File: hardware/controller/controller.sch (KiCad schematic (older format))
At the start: 7 parts

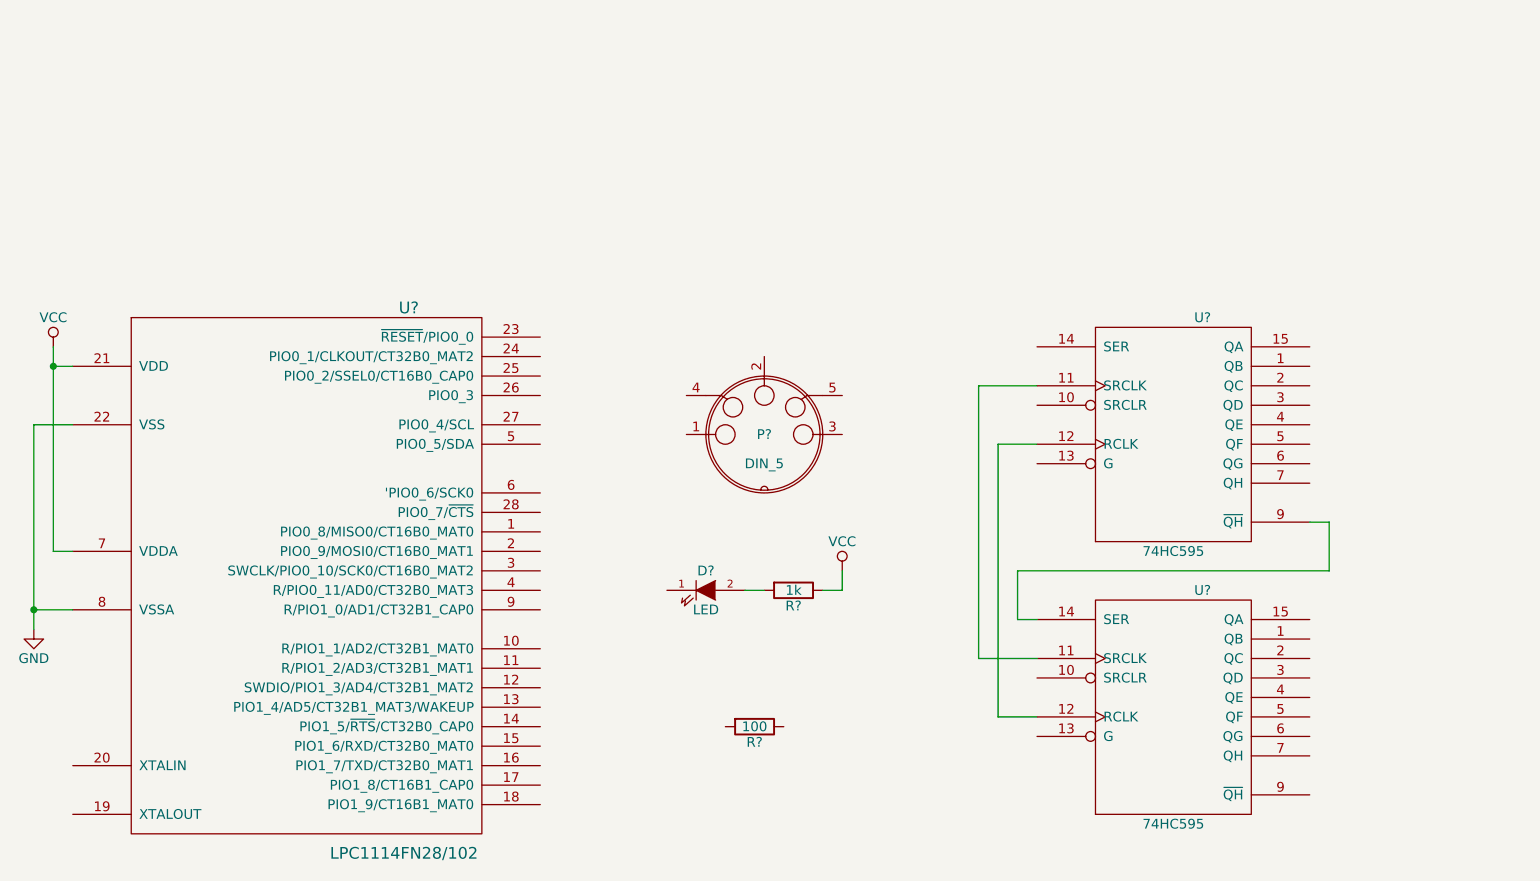
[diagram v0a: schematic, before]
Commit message: Add MIDI input and solenoid drive circuitry
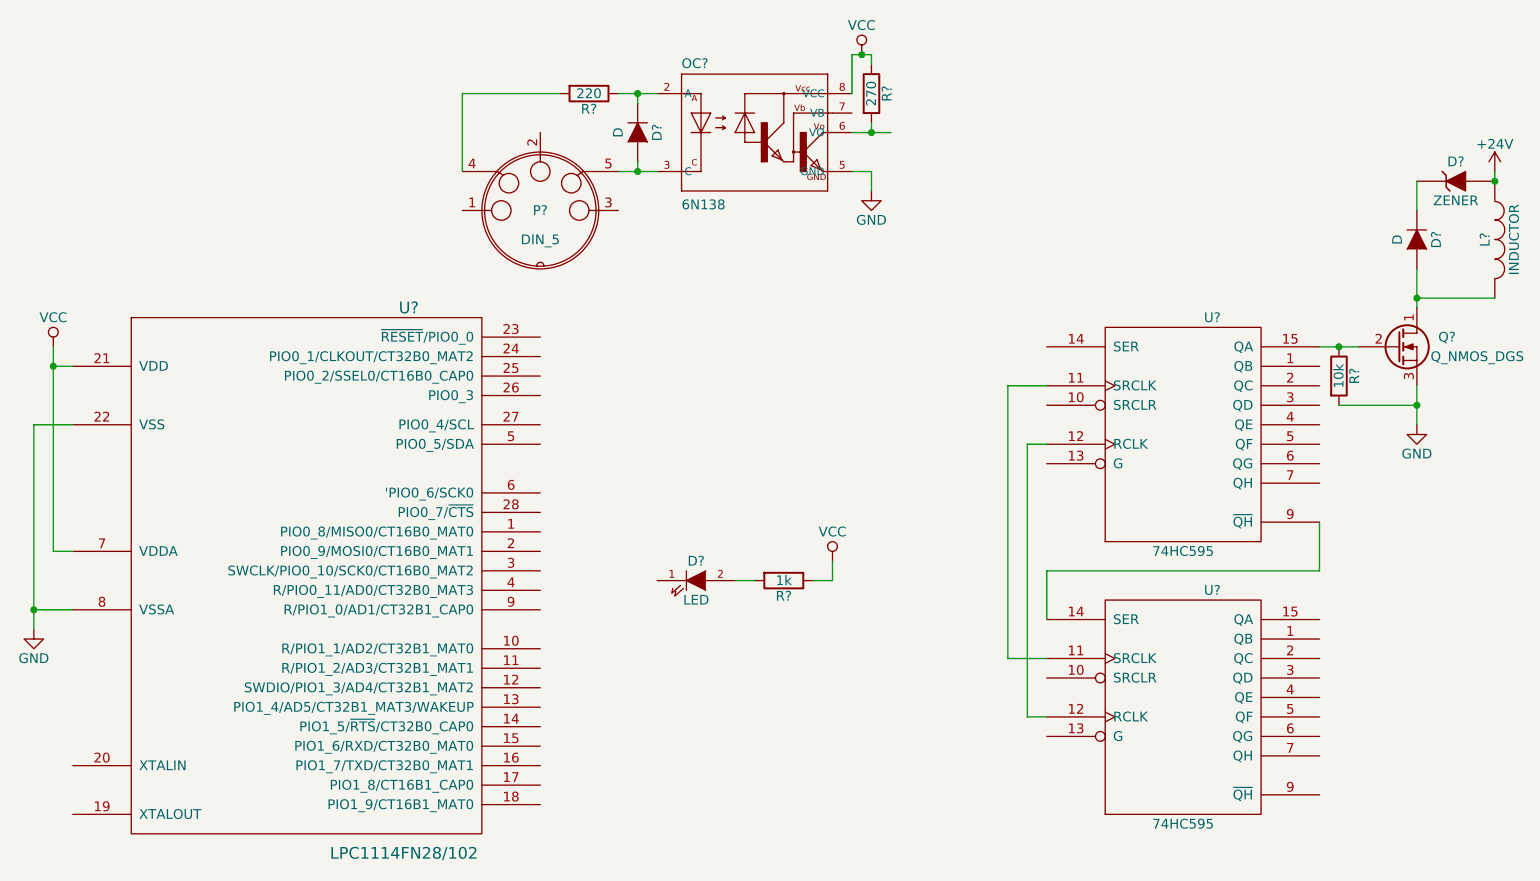
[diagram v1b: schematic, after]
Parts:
- added D? (x2): D, symbol D
- added D?: ZENER, symbol ZENER
- added L?: INDUCTOR, symbol INDUCTOR
- added OC?: 6N138, optocoupler-DIL08, symbol 6N138
- added Q?: Q_NMOS_DGS, symbol Q_NMOS_DGS
- added R?: 220, symbol R
- added R?: 10k, symbol R
- R?: value 100 -> 270
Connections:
- net GND: now also OC?.5 (GND), Q?.3 (S), R?.2
- net VCC: now also R?.1, OC?.8 (VCC)
- net at R?.2: now also OC?.6 (VO)
- net at P?.4: now also R?.2
- net at P?.5: now also D?.2 (A), OC?.3 (C)
- net at U?.15 (QA): now also Q?.2 (G), R?.1
- new net: D?.1 (K), OC?.2 (A), R?.1
- new net: D?.2 (A), L?.2, Q?.1 (D)
- new net: D?.1 (K), D?.1 (K)
- new net +24V: D?.2 (A), L?.1
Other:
- moved on the sheet: D?, P?, R?, U?
